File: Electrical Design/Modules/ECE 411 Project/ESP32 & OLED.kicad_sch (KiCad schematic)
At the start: 2 parts, among them U8 ESP32-C3-WROOM-02

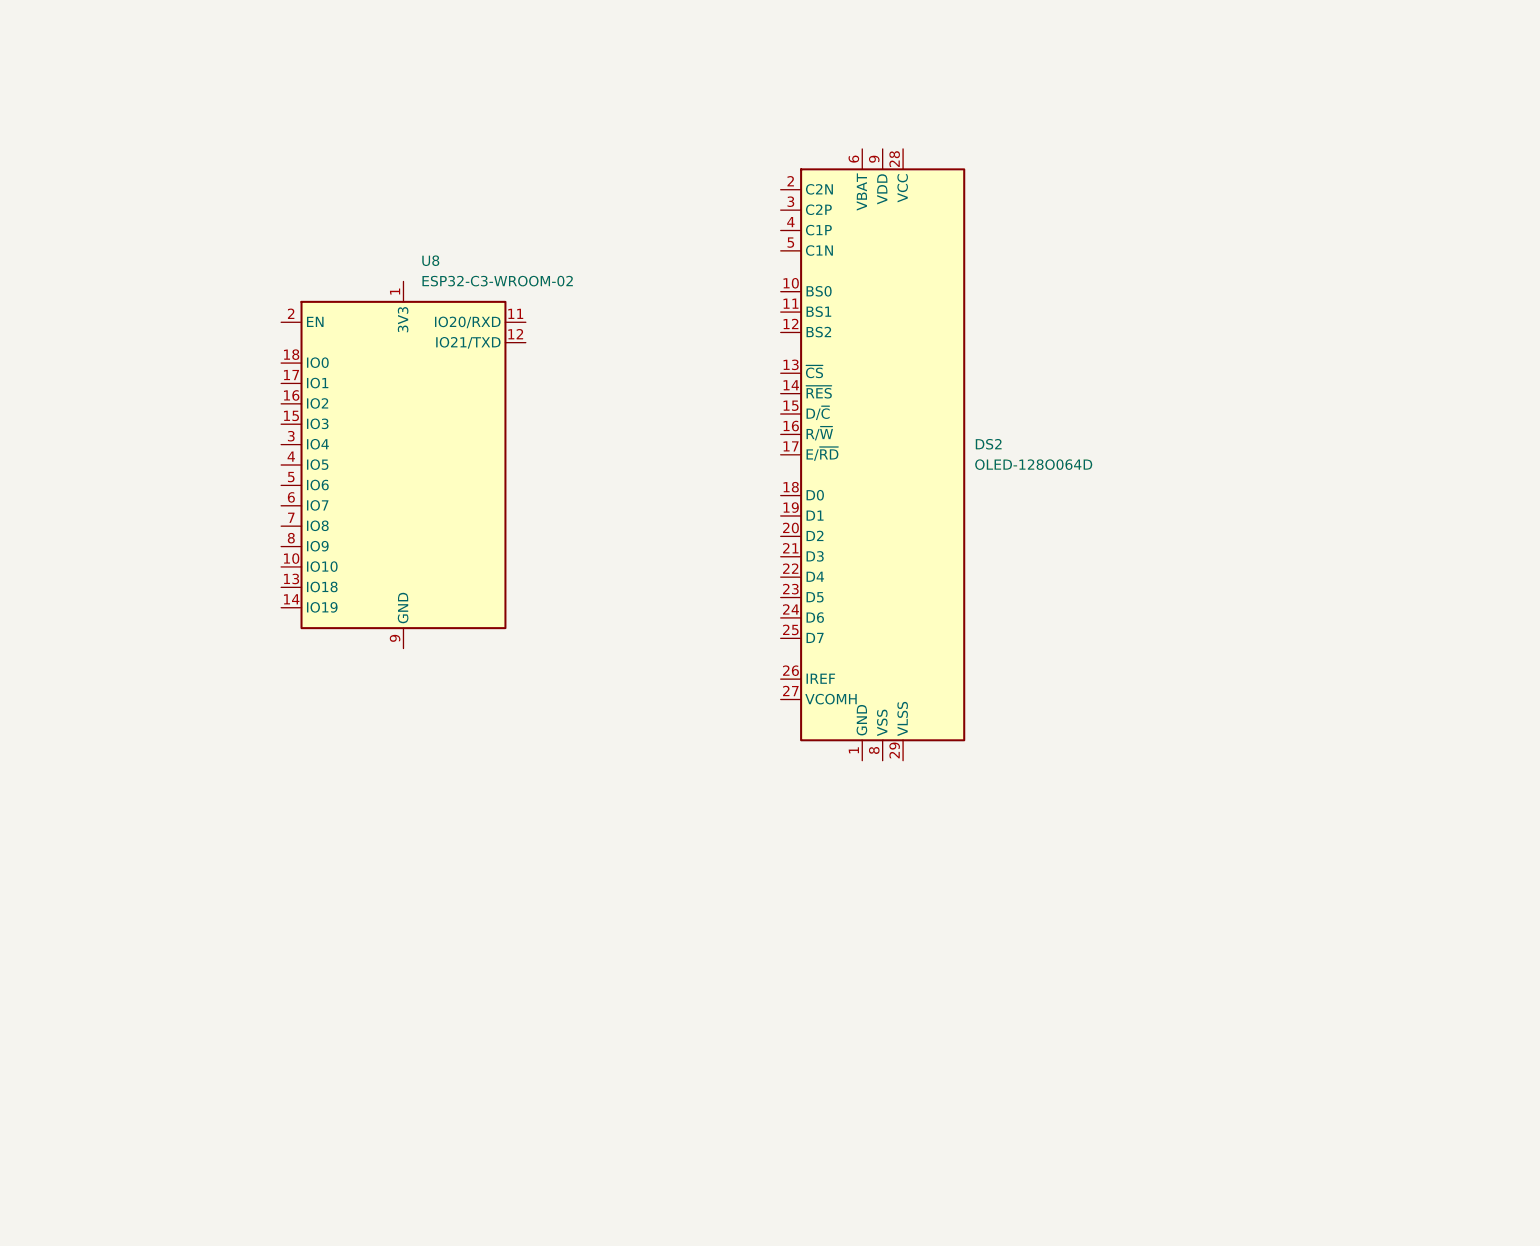
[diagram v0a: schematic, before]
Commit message: Minor changes to schematic wiring
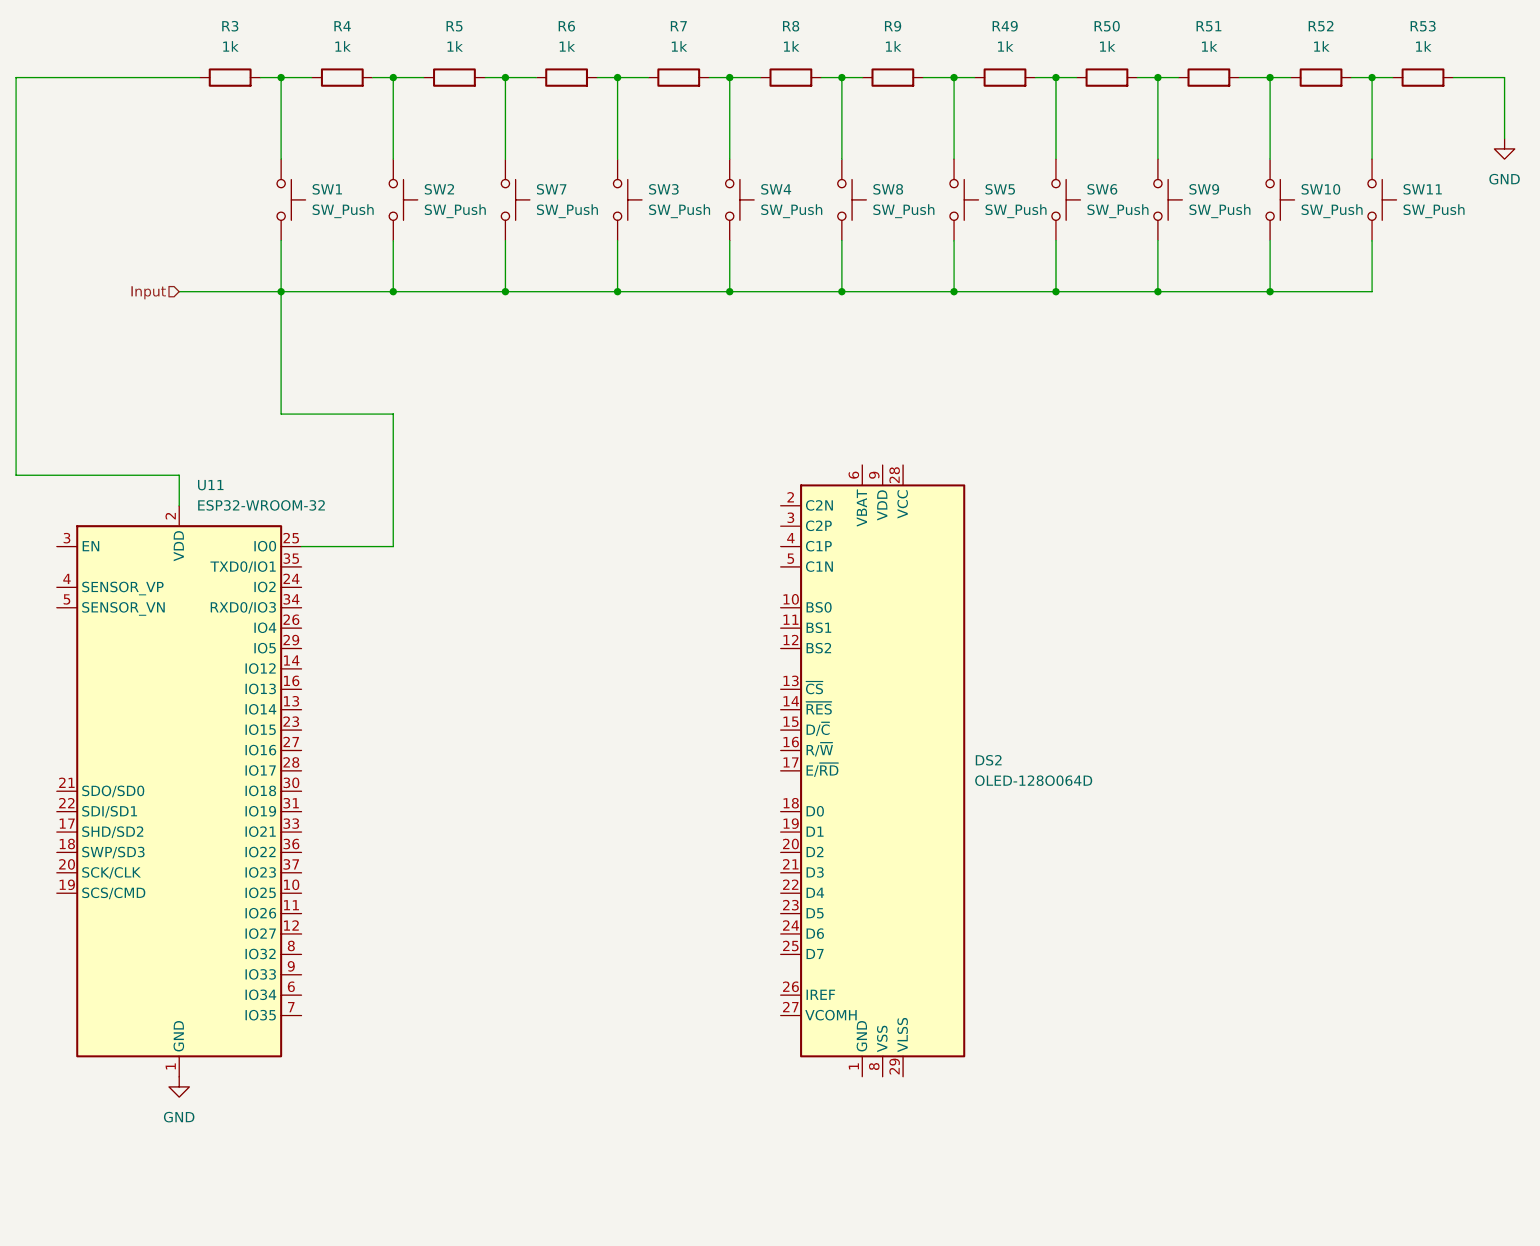
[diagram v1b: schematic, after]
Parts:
- removed U8: ESP32-C3-WROOM-02, RF_Module:ESP32-C3-WROOM-02, symbol RF_Module:ESP32-C3-WROOM-02
- added R3, R4, R49, R5, R50, R51, R52, R53, R6, R7, R8, R9: 1k, symbol Device:R
- added SW1, SW10, SW11, SW2, SW3, SW4, SW5, SW6, SW7, SW8, SW9: SW_Push, symbol Switch:SW_Push
- added U11: ESP32-WROOM-32, RF_Module:ESP32-WROOM-32, symbol RF_Module:ESP32-WROOM-32
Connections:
- new net: R3.2, R4.1, SW1.1
- new net: R4.2, R5.1, SW2.1
- new net: R8.2, R9.1, SW8.1
- new net: R7.2, R8.1, SW4.1
- new net: R51.2, R52.1, SW10.1
- new net: R52.2, R53.1, SW11.1
- new net: R6.2, R7.1, SW3.1
- new net: R50.2, R51.1, SW9.1
- new net: R49.1, R9.2, SW5.1
- new net: R5.2, R6.1, SW7.1
- new net: R49.2, R50.1, SW6.1
- new net: R3.1, U11.2 (VDD)
- new net GND: R53.2, U11.1 (GND), U11.15 (GND), U11.38 (GND), U11.39 (GND)
- new net Input: SW1.2, SW10.2, SW11.2, SW2.2, SW3.2, SW4.2, SW5.2, SW6.2, SW7.2, SW8.2, SW9.2, U11.25 (IO0)
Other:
- moved on the sheet: DS2

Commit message: Final Touches to Preliminary Schematic
Created Symbol for Small OLED screen and finalized input/output connections for each module
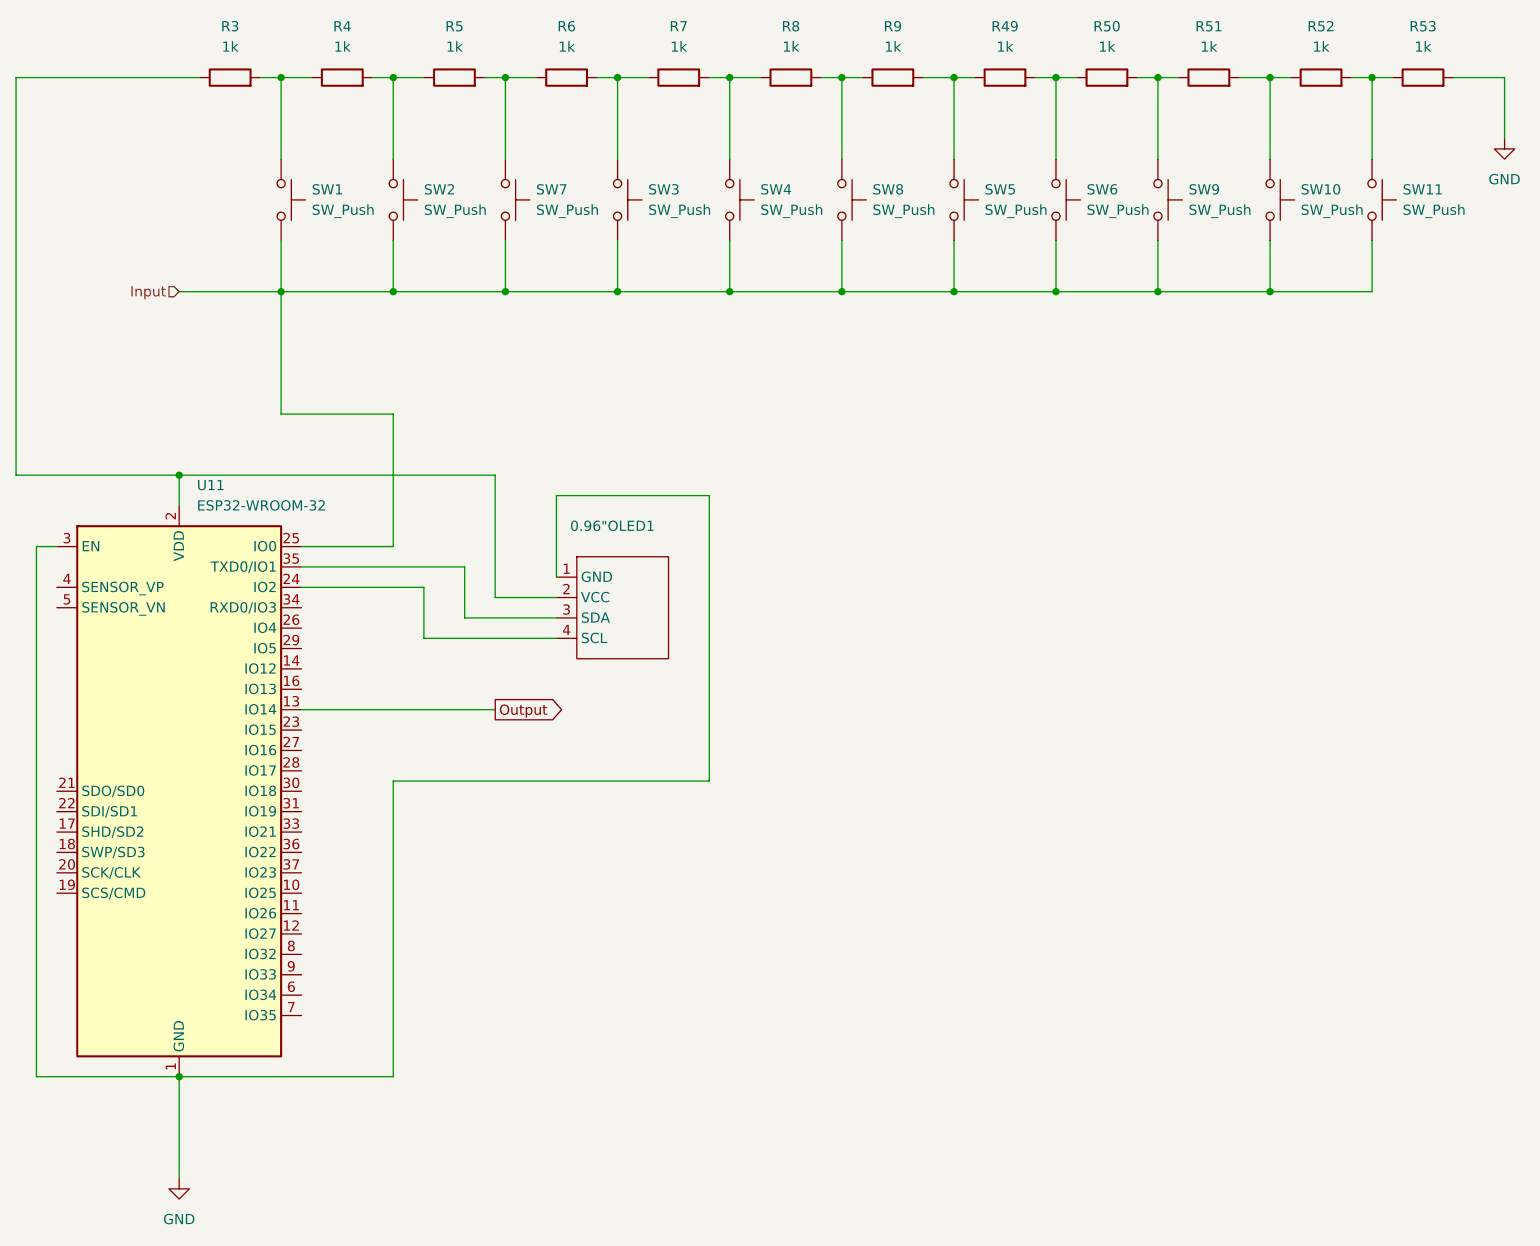
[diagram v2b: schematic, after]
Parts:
- removed DS2: OLED-128O064D, Display:OLED-128O064D, symbol Display_Graphic:OLED-128O064D
- added 0.96"OLED1: ~, symbol Project Specific Library:OLED_SSD1306
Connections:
- net GND: now also U11.3 (EN), 0.96"OLED1.1 (GND)
- net Output: now reaches U11.13 (IO14)
- net at R3.1, U11.2 (VDD): now also 0.96"OLED1.2 (VCC)
- net at U11.24 (IO2): now also 0.96"OLED1.4 (SCL)
- net at U11.35 (TXD0/IO1): now also 0.96"OLED1.3 (SDA)

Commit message: kicad business
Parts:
- removed 0.96"OLED1: ~, symbol Project Specific Library:OLED_SSD1306
- removed R3, R4, R49, R5, R50, R51, R52, R53, R6, R7, R8, R9: 1k, symbol Device:R
- removed SW1, SW10, SW11, SW2, SW3, SW4, SW5, SW6, SW7, SW8, SW9: SW_Push, symbol Switch:SW_Push
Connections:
- net +3V3: now reaches U11.2 (VDD)
- net IN: now reaches U11.23 (IO15)
- net SCL: now reaches U11.24 (IO2)
- net SDA: now reaches U11.35 (TXD0/IO1)
- net Input renamed IO0
- net Output renamed GENOUT
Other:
- company: (none) -> Portland State University
- title: (none) -> ESP32 Microcontroller Module
- moved on the sheet: U11

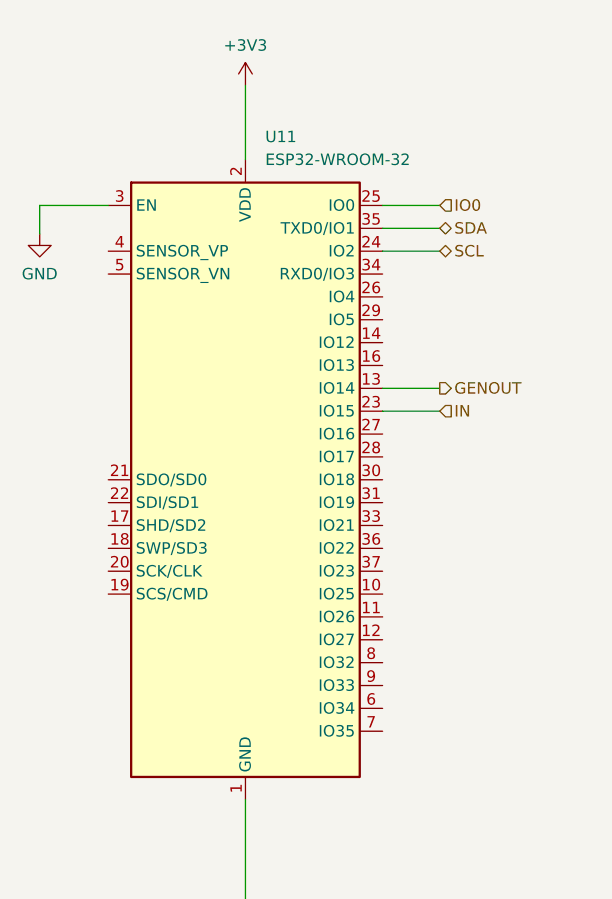
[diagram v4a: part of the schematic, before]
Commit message: schematic, start layout
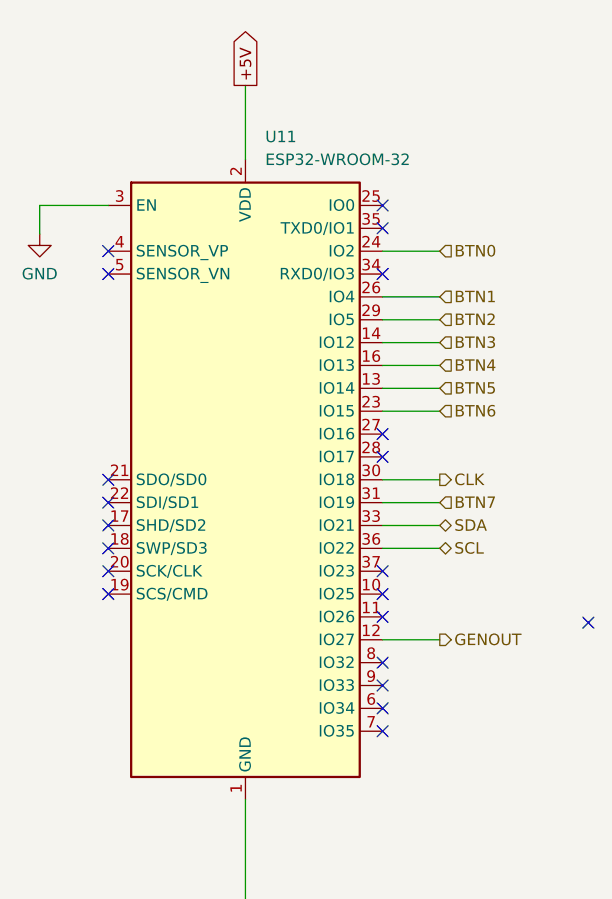
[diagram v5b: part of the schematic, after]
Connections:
- net GENOUT: now also U11.12 (IO27); no longer U11.13 (IO14)
- net SCL: now also U11.36 (IO22); no longer U11.24 (IO2)
- net SDA: now also U11.33 (IO21); no longer U11.35 (TXD0/IO1)
- net BTN3: now reaches U11.14 (IO12)
- net BTN4: now reaches U11.16 (IO13)
- net BTN1: now reaches U11.26 (IO4)
- net BTN2: now reaches U11.29 (IO5)
- net CLK: now reaches U11.30 (IO18)
- net BTN7: now reaches U11.31 (IO19)
- net +3V3 renamed +5V
- net IN renamed BTN6
- net IO0: no longer names the net of U11.25 (IO0)
- new net BTN0: U11.24 (IO2)
- new net BTN5: U11.13 (IO14)
- no-connect marks 0 -> 21

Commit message: update BOM
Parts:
- U11: Part Origin (none) -> SBP
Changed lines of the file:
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@@
+			)
+		)
+		(property "Part Number" ""
+			(at 144.145 92.075 0)
+			(effects
+				(font
+					(size 1.27 1.27)
+				)
+				(hide yes)
+			)
+		)
+		(property "Part Origin" "SBP"
+			(at 144.145 92.075 0)
+			(effects
+				(font
+					(size 1.27 1.27)
+				)
+				(hide yes)
+			)
+		)
+		(property "On Hand (On Way)" ""
+			(at 144.145 92.075 0)
+			(effects
+				(font
+					(size 1.27 1.27)
+				)
+				(hide yes)
 			)
 		)
